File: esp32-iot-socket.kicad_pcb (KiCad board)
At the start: 4 copper layers, 1 part, among them U1 ESP32-D0WDQ6

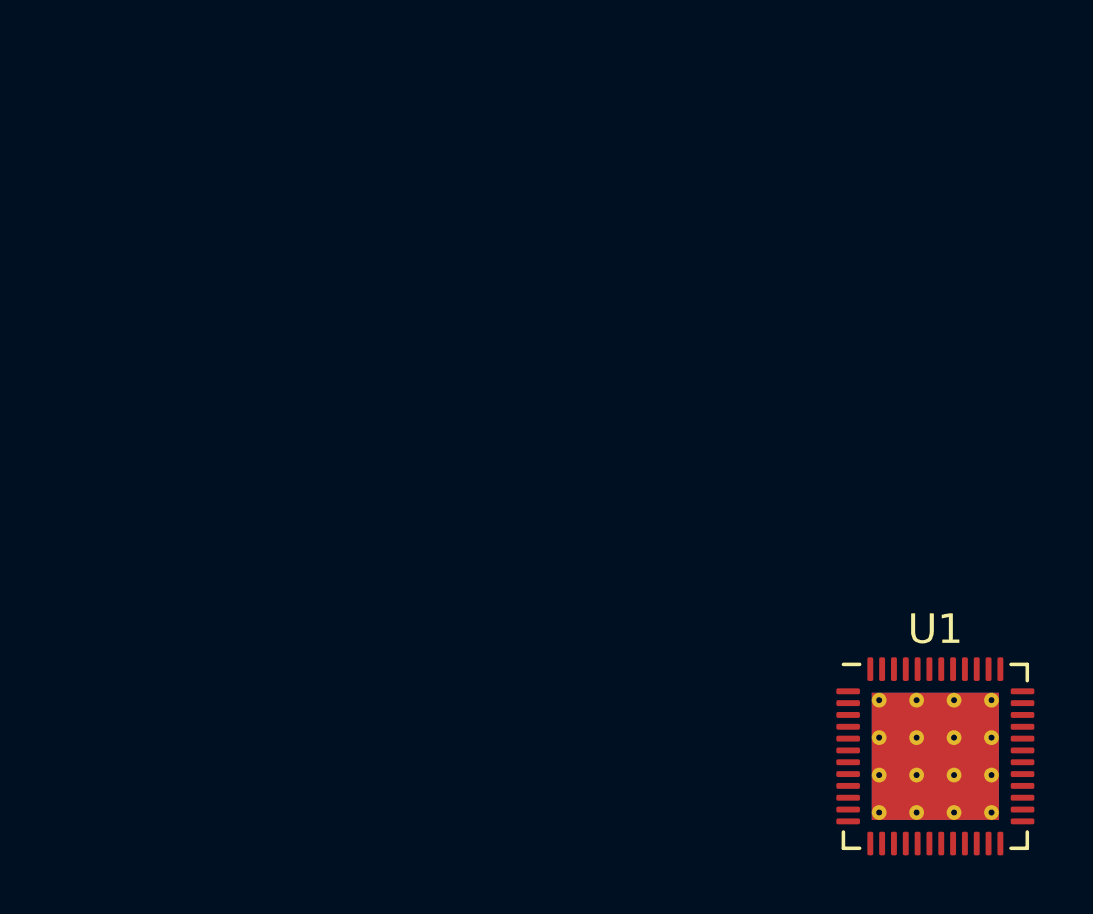
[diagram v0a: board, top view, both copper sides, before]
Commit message: progress in psu section:footprints added:flyback ic yet to be added
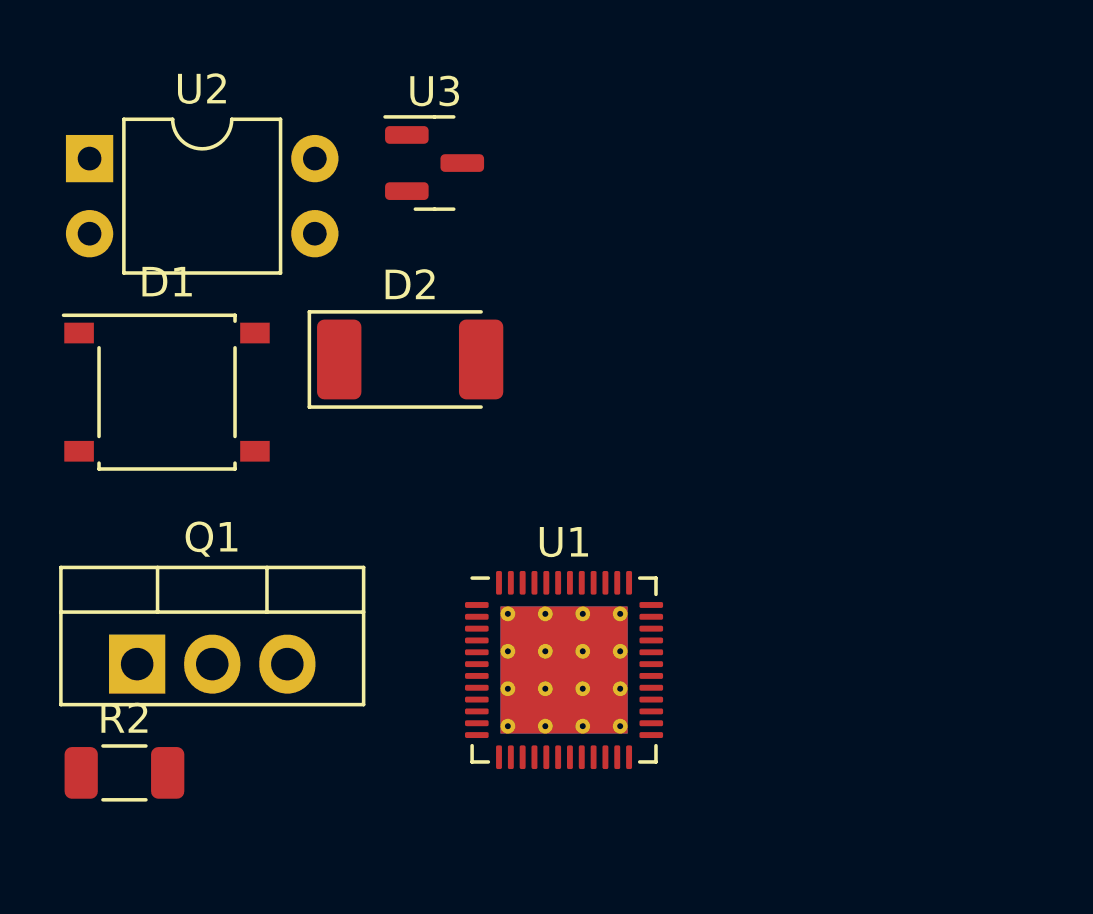
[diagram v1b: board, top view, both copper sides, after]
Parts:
- added D1: ABS10, Diode_SMD:Diode_Bridge_Diotec_ABS, F.Cu at (124.3, 87.4)
- added D2: SM4007, Diode_SMD:D_MELF, F.Cu at (132.5, 86.3)
- added Q1: BT136-800, Package_TO_SOT_THT:TO-220-3_Vertical, F.Cu at (123.3, 96.6)
- added R2: 470, Resistor_SMD:R_1206_3216Metric, F.Cu at (122.9, 100.3)
- added U2: PC817, Package_DIP:DIP-4_W7.62mm, F.Cu at (121.7, 79.5)
- added U3: TL431DBZ, Package_TO_SOT_SMD:SOT-23, F.Cu at (133.3, 79.7)
- moved U1 12.9 mm to (137.7, 96.8)

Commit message: schematic completed:
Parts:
- added C1: 104J 400V, Capacitor_THT:C_Rect_L10.3mm_W4.5mm_P7.50mm_MKS4, F.Cu at (129.1, 116.2)
- added C10: 100nF, Capacitor_SMD:C_1206_3216Metric, F.Cu at (162.0, 83.4)
- added C11: 100nF, Capacitor_SMD:C_1206_3216Metric, F.Cu at (162.0, 86.8)
- added C12: 100nF, Capacitor_SMD:C_1206_3216Metric, F.Cu at (162.0, 90.1)
- added C13: 100nF, Capacitor_SMD:C_1206_3216Metric, F.Cu at (162.0, 93.5)
- added C14: 10uF, Capacitor_Tantalum_SMD:CP_EIA-6032-20_AVX-F_Pad2.25x2.35mm_HandSolder, F.Cu at (186.0, 95.0)
- added C15: 10pF, Capacitor_SMD:C_0603_1608Metric_Pad1.08x0.95mm_HandSolder, F.Cu at (167.0, 76.3)
- added C16: 10pF, Capacitor_SMD:C_0603_1608Metric_Pad1.08x0.95mm_HandSolder, F.Cu at (167.0, 78.8)
- added C17: 100nF, Capacitor_SMD:C_1206_3216Metric, F.Cu at (162.0, 96.8)
- added C18: 100nF, Capacitor_SMD:C_1206_3216Metric, F.Cu at (162.0, 100.2)
- added C19: 4.7uF, Capacitor_Tantalum_SMD:CP_EIA-6032-20_AVX-F_Pad2.25x2.35mm_HandSolder, F.Cu at (186.0, 99.8)
- added C2: 2.2uF 400V, Capacitor_THT:CP_Radial_D8.0mm_P3.50mm, F.Cu at (130.1, 108.4)
- added C20: 100nF, Capacitor_SMD:C_1206_3216Metric, F.Cu at (162.0, 103.5)
- added C21: 3.3pF, Capacitor_SMD:C_0402_1005Metric, F.Cu at (23.4, 67.8)
- added C22: 3.3pF, Capacitor_SMD:C_0402_1005Metric, F.Cu at (23.4, 71.1)
- added C3: 470uF 10V, Capacitor_SMD:CP_Elec_5x5.3, F.Cu at (145.0, 112.3)
- added C4: 2.2uF 50V, Capacitor_THT:CP_Radial_D5.0mm_P2.50mm, F.Cu at (117.3, 112.3)
- added C5: 102, Capacitor_THT:C_Rect_L4.6mm_W2.0mm_P2.50mm_MKS02_FKP02, F.Cu at (150.8, 80.9)
- added C6: 47nF, Capacitor_SMD:C_01005_0402Metric_Pad0.57x0.30mm_HandSolder, F.Cu at (147.6, 116.6)
- added C7: 102 2kV Y1, Capacitor_THT:C_Disc_D5.0mm_W2.5mm_P5.00mm, F.Cu at (150.6, 77.1)
- added C8: 100nF, Capacitor_SMD:C_1206_3216Metric, F.Cu at (162.0, 76.7)
- added C9: 100nF, Capacitor_SMD:C_1206_3216Metric, F.Cu at (162.0, 80.1)
- added D3: B150-E3, Diode_SMD:D_SMA, F.Cu at (150.2, 91.4)
- added D4: 1N4148W, Diode_SMD:D_SOD-123, F.Cu at (143.4, 117.4)
- added D5: SM4007, Diode_SMD:D_MELF, F.Cu at (144.5, 106.7)
- added F1: 0.5W 10, Resistor_THT:R_Axial_DIN0411_L9.9mm_D3.6mm_P15.24mm_Horizontal, F.Cu at (128.9, 91.7)
- added J3: Screw_Terminal_01x03, TerminalBlock_Phoenix:TerminalBlock_Phoenix_MKDS-1,5-3-5.08_1x03_P5.08mm_Horizontal, F.Cu at (135.3, 81.3)
- added L1: 2.2nH, Inductor_SMD:L_1210_3225Metric_Pad1.42x2.65mm_HandSolder, F.Cu at (184.4, 104.2)
- added L2: 2.2nH, Inductor_SMD:L_0402_1005Metric_Pad0.77x0.64mm_HandSolder, F.Cu at (23.9, 69.4)
- added R1: 1.5k, Resistor_SMD:R_0402_1005Metric, F.Cu at (123.2, 110.0)
- added R10: 22, Resistor_SMD:R_0603_1608Metric_Pad0.98x0.95mm_HandSolder, F.Cu at (167.0, 81.3)
- added R11: 5.1k, Resistor_SMD:R_0603_1608Metric_Pad0.98x0.95mm_HandSolder, F.Cu at (167.0, 83.9)
- added R12: 5.1k, Resistor_SMD:R_0603_1608Metric_Pad0.98x0.95mm_HandSolder, F.Cu at (167.0, 86.4)
- added R13: 22, Resistor_SMD:R_0603_1608Metric_Pad0.98x0.95mm_HandSolder, F.Cu at (167.0, 88.9)
- added R14: 22, Resistor_SMD:R_0603_1608Metric_Pad0.98x0.95mm_HandSolder, F.Cu at (167.0, 91.4)
- added R15: 470, Resistor_SMD:R_0603_1608Metric_Pad0.98x0.95mm_HandSolder, F.Cu at (171.3, 76.3)
- added R16: 470, Resistor_SMD:R_0603_1608Metric_Pad0.98x0.95mm_HandSolder, F.Cu at (171.3, 78.8)
- added R17: 22, Resistor_SMD:R_0603_1608Metric_Pad0.98x0.95mm_HandSolder, F.Cu at (171.3, 81.3)
- added R18: 22, Resistor_SMD:R_0603_1608Metric_Pad0.98x0.95mm_HandSolder, F.Cu at (171.3, 83.9)
- added R19: 22, Resistor_SMD:R_0603_1608Metric_Pad0.98x0.95mm_HandSolder, F.Cu at (171.3, 86.4)
- added R20: 68k, Resistor_SMD:R_0603_1608Metric_Pad0.98x0.95mm_HandSolder, F.Cu at (171.3, 88.9)
- added R21: 68k, Resistor_SMD:R_0603_1608Metric_Pad0.98x0.95mm_HandSolder, F.Cu at (171.3, 91.4)
- added R22: 68k, Resistor_SMD:R_0603_1608Metric_Pad0.98x0.95mm_HandSolder, F.Cu at (175.7, 76.3)
- added R23: 68k, Resistor_SMD:R_0603_1608Metric_Pad0.98x0.95mm_HandSolder, F.Cu at (175.7, 78.8)
- added R24: 68k, Resistor_SMD:R_0603_1608Metric_Pad0.98x0.95mm_HandSolder, F.Cu at (175.7, 81.3)
- added R25: 22, Resistor_SMD:R_0603_1608Metric_Pad0.98x0.95mm_HandSolder, F.Cu at (175.7, 83.9)
- added R3: 470, Resistor_SMD:R_0402_1005Metric, F.Cu at (123.2, 112.0)
- added R4: 4.7k, Resistor_SMD:R_0402_1005Metric, F.Cu at (123.2, 114.0)
- added R5: 470, Resistor_SMD:R_0402_1005Metric, F.Cu at (123.2, 116.0)
- added R6: 82k, Resistor_SMD:R_1206_3216Metric_Pad1.30x1.75mm_HandSolder, F.Cu at (118.1, 117.2)
- added R7: 150k, Resistor_SMD:R_1206_3216Metric, F.Cu at (152.3, 113.8)
- added R8: 150k, Resistor_SMD:R_1206_3216Metric, F.Cu at (152.3, 117.1)
- added R9: 1.5k, Resistor_SMD:R_0402_1005Metric, F.Cu at (123.2, 118.0)
- added SW1: Reset, Button_Switch_SMD:SW_SPST_B3U-1000P-B, F.Cu at (225.6, 102.8)
- added SW2: Boot, Button_Switch_SMD:SW_SPST_B3U-1000P-B, F.Cu at (225.6, 107.1)
- added T2: POE30P-33L, footprint:POE30P33L, F.Cu at (123.4, 82.1)
- added TP1: 3.3V, TestPoint:TestPoint_Pad_D1.5mm, F.Cu at (166.6, 101.5)
- added TP2: GND, TestPoint:TestPoint_Pad_D1.5mm, F.Cu at (166.6, 105.1)
- added TP3: Rx, TestPoint:TestPoint_Pad_D1.5mm, F.Cu at (170.1, 101.5)
- added TP4: Tx, TestPoint:TestPoint_Pad_D1.5mm, F.Cu at (170.1, 105.1)
- added TP5: DTR, TestPoint:TestPoint_Pad_D1.5mm, F.Cu at (173.7, 101.5)
- added TP6: RTS, TestPoint:TestPoint_Pad_D1.5mm, F.Cu at (173.7, 105.1)
- added U4: MOC3021M, Package_DIP:DIP-6_W8.89mm_SMDSocket_LongPads, F.Cu at (133.7, 98.9)
- added U5: VIPer22AS, Package_SO:SOIC-8_3.9x4.9mm_P1.27mm, F.Cu at (119.4, 105.8)
- added U6: PC817, Package_DIP:DIP-4_W7.62mm_SMDSocket_SmallPads, F.Cu at (121.0, 99.2)
- added U7: W25Q32JVSS, Package_SO:SOIC-8_5.23x5.23mm_P1.27mm, F.Cu at (230.8, 91.3)
- added U8: ANTENNA 2.4GHz, RF_Antenna:Texas_SWRA117D_2.4GHz_Right, F.Cu at (23.9, 66.7)
- added Y1: ABM10AIG, Oscillator:Oscillator_SMD_Abracon_ASDMB-4Pin_2.5x2.0mm, F.Cu at (189.4, 104.1)
- U2: footprint Package_DIP:DIP-4_W7.62mm -> Package_DIP:DIP-4_W7.62mm_SMDSocket_SmallPads
- moved U1 78.4 mm to (216.0, 91.2)
- moved D1 32.6 mm to (152.6, 103.5)
- moved R2 31.1 mm to (152.3, 110.5)
- moved Q1 20.5 mm to (143.7, 98.2)
- moved D2 20.0 mm to (144.5, 102.4)
- moved U3 18.9 mm to (151.5, 84.9)
- moved U2 13.0 mm to (121.0, 92.5)
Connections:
- D1 pad 1: unconnected-(D1-+-Pad1) -> Net-(D1-+)
- D1 pad 2: unconnected-(D1---Pad2) -> Net-(D1--)
- D1 pad 3: unconnected-(D1-Pad3) -> Net-(J3-Pin_2)
- D1 pad 4: unconnected-(D1-Pad4) -> Net-(C1-Pad1)
- D2 pad 1: unconnected-(D2-K-Pad1) -> Net-(D2-K)
- D2 pad 2: unconnected-(D2-A-Pad2) -> Net-(D2-A)
- Q1 pad 1: unconnected-(Q1-A1-Pad1) -> /Power Supply Section/L
- Q1 pad 2: unconnected-(Q1-A2-Pad2) -> Net-(J3-Pin_3)
- Q1 pad 3: unconnected-(Q1-G-Pad3) -> Net-(Q1-G)
- R2 pad 1: unconnected-(R2-Pad1) -> Net-(Q1-G)
- R2 pad 2: unconnected-(R2-Pad2) -> Net-(R2-Pad2)
- U1 pad 1: unconnected-(U1B-VDDA-Pad1) -> +3V3
- U1 pad 16: unconnected-(U1A-GPIO27-Pad16) -> /Microcontroller Section/ZVC signal in
- U1 pad 18: unconnected-(U1A-MTDI-Pad18) -> Net-(U1A-MTDI)
- U1 pad 19: unconnected-(U1B-VDD3P3_RTC-Pad19) -> +3V3
- U1 pad 2: unconnected-(U1A-LNA_IN-Pad2) -> Net-(U1A-LNA_IN)
- U1 pad 20: unconnected-(U1A-MTCK-Pad20) -> Net-(U1A-MTCK)
- U1 pad 21: unconnected-(U1A-MTDO-Pad21) -> Net-(U1A-MTDO)
- U1 pad 22: unconnected-(U1A-GPIO2-Pad22) -> Net-(U1A-GPIO2)
- U1 pad 23: unconnected-(U1A-GPIO0-Pad23) -> /Microcontroller Section/Boot
- U1 pad 25: unconnected-(U1A-GPIO16-Pad25) -> Net-(U1A-GPIO16)
- U1 pad 26: unconnected-(U1B-VDD_SDIO-Pad26) -> /Microcontroller Section/VDD_SDIO
- U1 pad 28: unconnected-(U1A-SD_DATA_2-Pad28) -> /Microcontroller Section/SHD/SD2
- U1 pad 29: unconnected-(U1A-SD_DATA_3-Pad29) -> /Microcontroller Section/SWP/SD3
- U1 pad 3: unconnected-(U1B-VDD3P3-Pad3) -> /Microcontroller Section/3.3V RF
- U1 pad 30: unconnected-(U1A-SD_CMD-Pad30) -> /Microcontroller Section/SCS/CMD
- U1 pad 31: unconnected-(U1A-SD_CLK-Pad31) -> /Microcontroller Section/SCK/CLK
- U1 pad 32: unconnected-(U1A-SD_DATA_0-Pad32) -> /Microcontroller Section/SDO/SD0
- U1 pad 33: unconnected-(U1A-SD_DATA_1-Pad33) -> /Microcontroller Section/SDI/SD1
- U1 pad 34: unconnected-(U1A-GPIO5-Pad34) -> Net-(U1A-GPIO5)
- U1 pad 37: unconnected-(U1B-VDD3P3_CPU-Pad37) -> +3V3
- U1 pad 4: unconnected-(U1B-VDD3P3-Pad4) -> /Microcontroller Section/3.3V RF
- U1 pad 40: unconnected-(U1A-U0RXD-Pad40) -> /Microcontroller Section/Rx
- U1 pad 41: unconnected-(U1A-U0TXD-Pad41) -> /Microcontroller Section/Tx
- U1 pad 43: unconnected-(U1B-VDDA-Pad43) -> +3V3
- U1 pad 44: unconnected-(U1A-XTAL_N-Pad44) -> /Microcontroller Section/XTal_N
- U1 pad 45: unconnected-(U1A-XTAL_P-Pad45) -> /Microcontroller Section/XTal_P
- U1 pad 46: unconnected-(U1B-VDDA-Pad46) -> +3V3
- U1 pad 49: unconnected-(U1B-GND-Pad49) -> GNDD
- U1 pad 9: unconnected-(U1A-CHIP_PU-Pad9) -> /Microcontroller Section/DTR
- U2 pad 1: unconnected-(U2-Pad1) -> Net-(R5-Pad2)
- U2 pad 2: unconnected-(U2-Pad2) -> Net-(U3-K)
- U2 pad 3: unconnected-(U2-Pad3) -> Net-(U5-FB)
- U2 pad 4: unconnected-(U2-Pad4) -> Net-(D4-K)
- U3 pad 1: unconnected-(U3-K-Pad1) -> Net-(U3-K)
- U3 pad 2: unconnected-(U3-REF-Pad2) -> Net-(U3-REF)
- U3 pad 3: unconnected-(U3-A-Pad3) -> GNDD
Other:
- board outline added: 25 x 50 mm
